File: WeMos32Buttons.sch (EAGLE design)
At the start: 9 parts, among them J1 Digital_8_13, J3 Digital_8_13

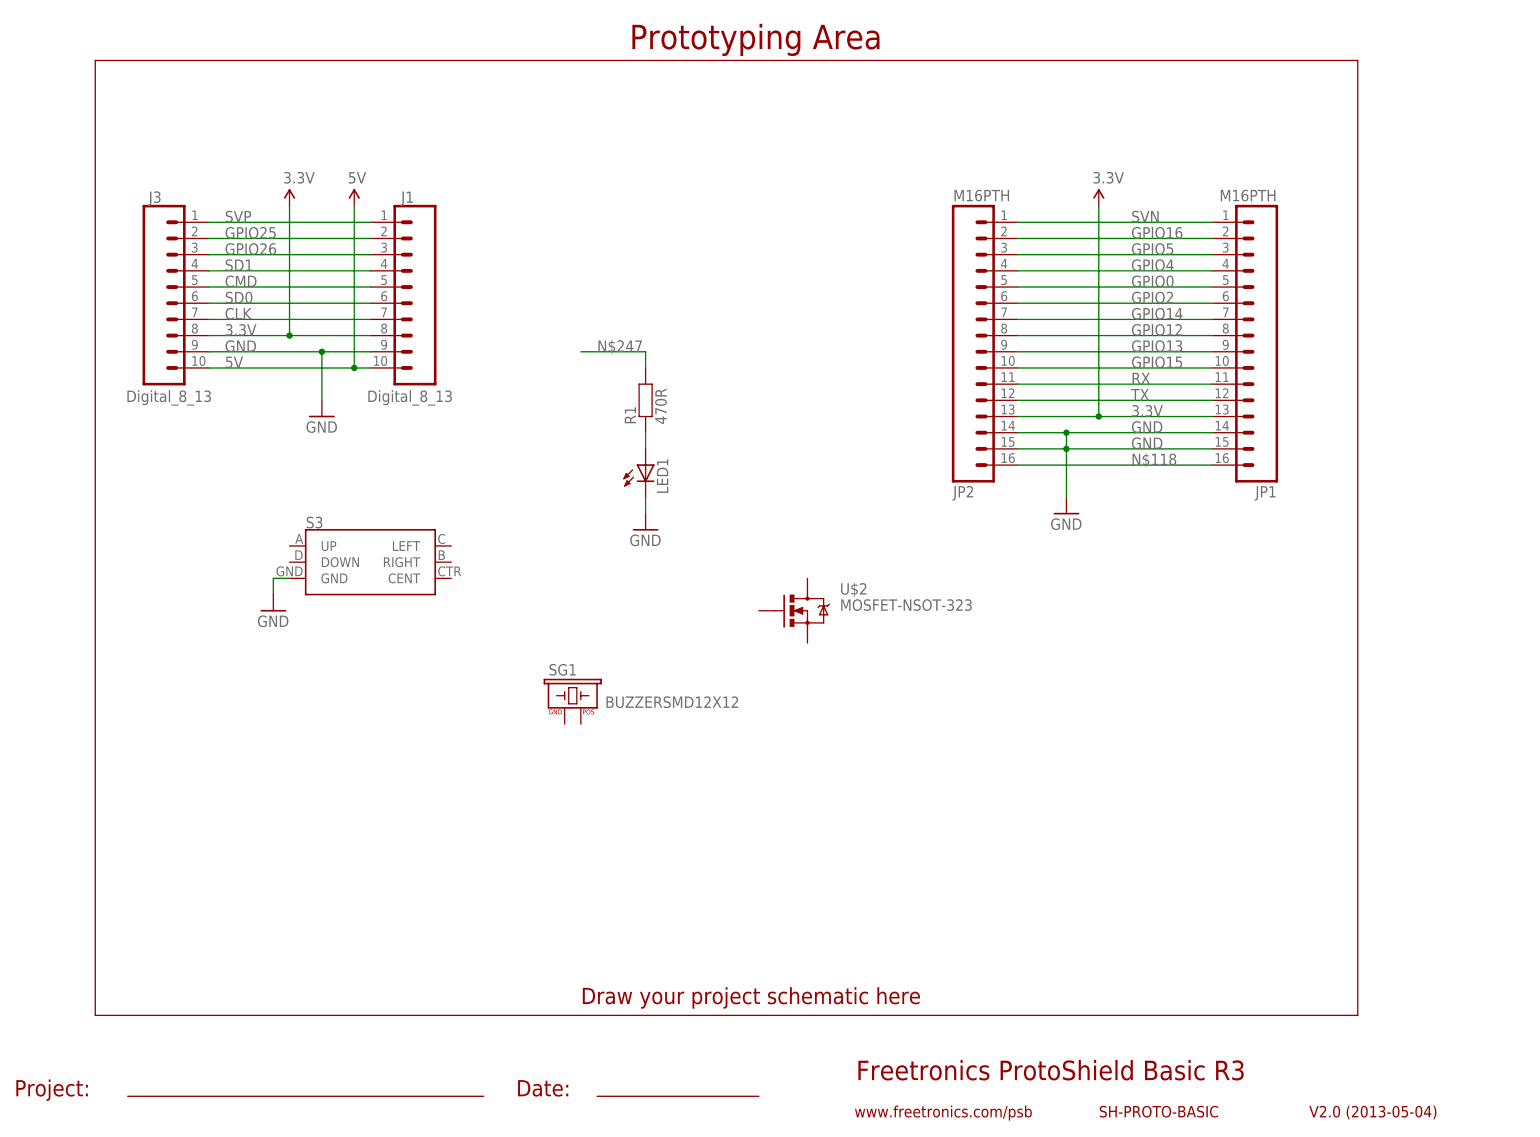
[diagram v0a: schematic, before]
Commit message: Added pull-ups on all inputs, restructured to fit fake WeMos board
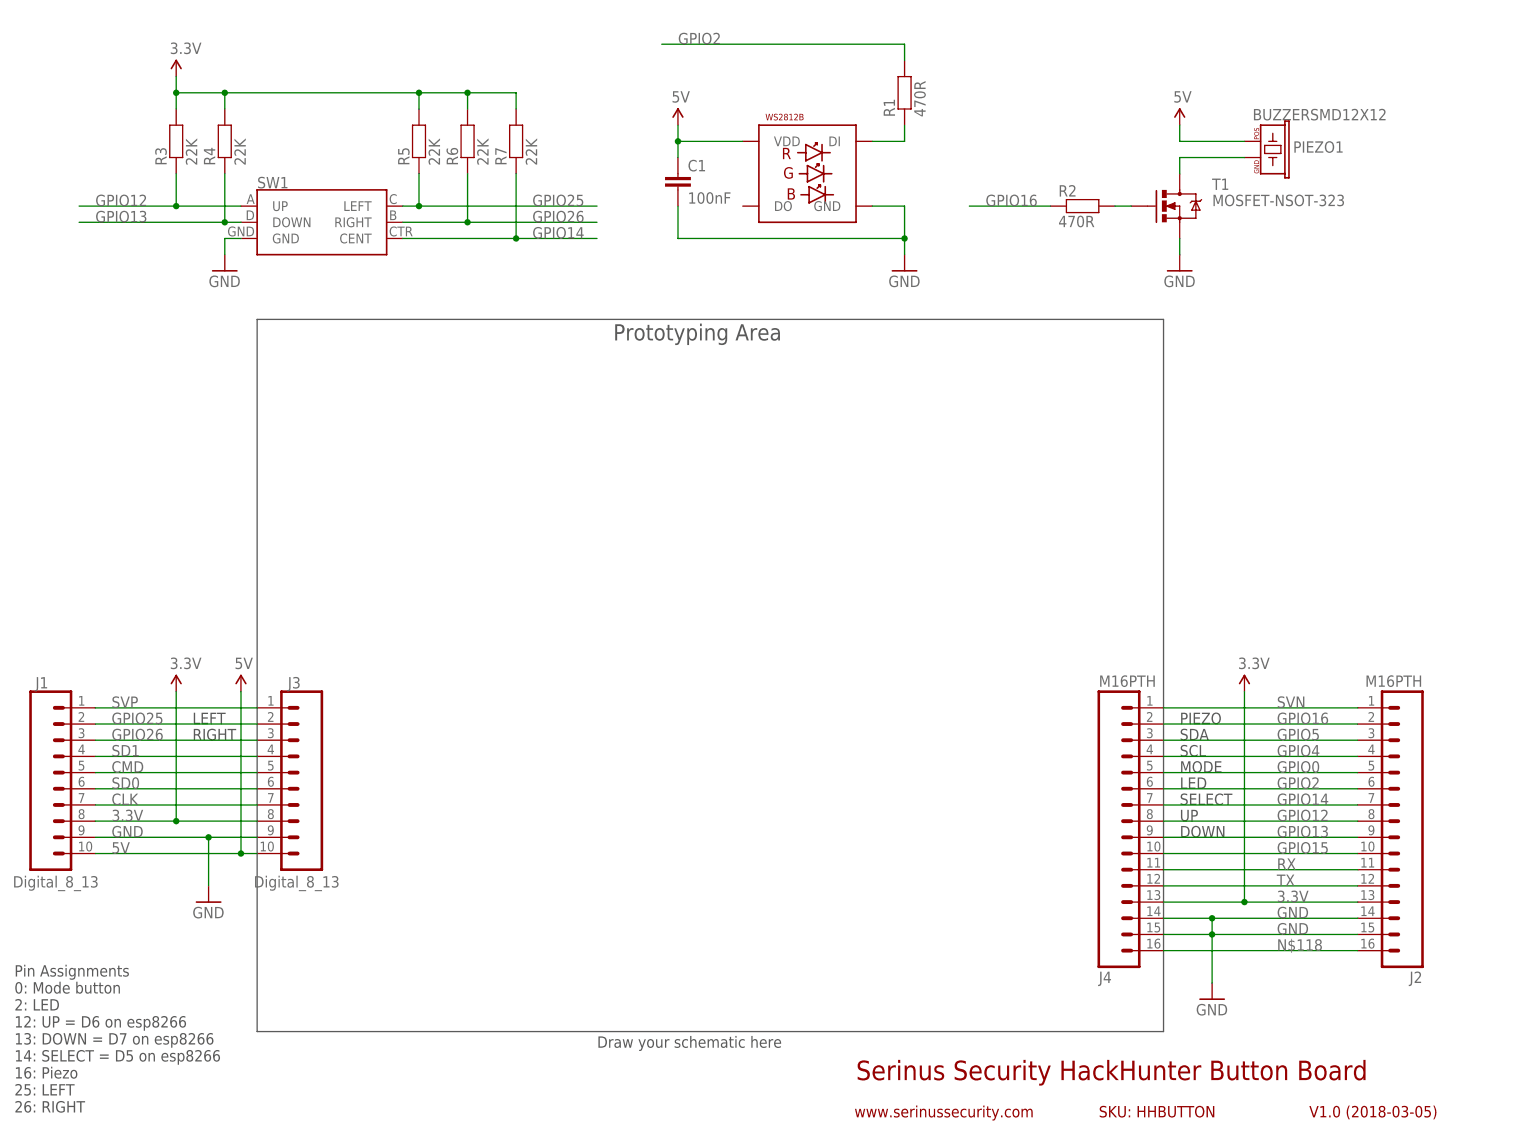
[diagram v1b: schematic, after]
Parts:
- removed JP1, JP2: M16PTH, freetronics-jon:M16PTH
- removed LED1: (no value), freetronics-jon:LED3MM
- removed S3: (no value), SparkFun-Switches:JOYSTICK_MINI
- removed SG1: BUZZERSMD12X12, freetronics-master-v1.1:BUZZERSMD12X12
- removed U$2: MOSFET-NSOT-323, freetronics-jon:MOSFET-NSOT-323
- added C1: 100nF, freetronics-jon:CAP0603
- added J2, J4: M16PTH, freetronics-jon:M16PTH
- added LED2: WS2812B5050, freetronics-jon:WS2812B5050
- added PIEZO1: BUZZERSMD12X12, freetronics-master-v1.1:BUZZERSMD12X12
- added R2: 470R, freetronics-jon:RESISTOR0603
- added R3, R4, R5, R6, R7: 22K, freetronics-jon:RESISTOR0603
- added SW1: (no value), SparkFun-Switches:JOYSTICK_MINI
- added T1: MOSFET-NSOT-323, freetronics-jon:MOSFET-NSOT-323
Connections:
- removed net N$247: R1.2
- new net N$8: PIEZO1.GND, T1.D
- new net N$9: R2.2, T1.G
- net 3.3V: now also J2.13, J4.13, R3.2, R4.2, R5.2, R6.2, R7.2; no longer JP1.13, JP2.13
- net 5V: now also C1.1, LED2.VDD, PIEZO1.POS
- net GND: now also C1.2, J2.14, J2.15, J4.14, J4.15, LED2.GND, SW1.GND, T1.S; no longer JP1.14, JP1.15, JP2.14, JP2.15, LED1.C, S3.GND
- net GPIO0: now also J2.5, J4.5; no longer JP1.5, JP2.5
- net GPIO12: now also J2.8, J4.8, R3.1, SW1.UP; no longer JP1.8, JP2.8
- net GPIO13: now also J2.9, J4.9, R4.1, SW1.DOWN; no longer JP1.9, JP2.9
- net GPIO14: now also J2.7, J4.7, R7.1, SW1.CENT; no longer JP1.7, JP2.7
- net GPIO15: now also J2.10, J4.10; no longer JP1.10, JP2.10
- net GPIO16: now also J2.2, J4.2, R2.1; no longer JP1.2, JP2.2
- net GPIO2: now also J2.6, J4.6, R1.2; no longer JP1.6, JP2.6
- net GPIO25: now also R5.1, SW1.LEFT
- net GPIO26: now also R6.1, SW1.RIGHT
- net GPIO4: now also J2.4, J4.4; no longer JP1.4, JP2.4
- net GPIO5: now also J2.3, J4.3; no longer JP1.3, JP2.3
- net N$118: now also J2.16, J4.16; no longer JP1.16, JP2.16
- net N$246: now also LED2.DI; no longer LED1.A
- net RX: now also J2.11, J4.11; no longer JP1.11, JP2.11
- net SVN: now also J2.1, J4.1; no longer JP1.1, JP2.1
- net TX: now also J2.12, J4.12; no longer JP1.12, JP2.12
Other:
- note added: "DOWN"
- note added: "Draw your schematic here"
- note added: "LED"
- note added: "LEFT"
- note added: "MODE"
- note added: "PIEZO"
- note added: "Pin Assignments 0: Mode button 2: LED 12: UP = D6 on esp8266 13: DOWN = D7 on esp8266 14: SELECT = D5 on esp8266 16: Piezo 25: LEFT 26: RIGHT"
- note added: "RIGHT"
- note added: "SCL"
- note added: "SDA"
- note added: "SELECT"
- note added: "SKU: HHBUTTON"
- note added: "Serinus Security HackHunter Button Board"
- note added: "UP"
- note added: "V1.0 (2018-03-05)"
- note added: "www.serinussecurity.com"
- note removed: "Date:"
- note removed: "Draw your project schematic here"
- note removed: "Freetronics ProtoShield Basic R3"
- note removed: "Project:"
- note removed: "SH-PROTO-BASIC"
- note removed: "V2.0 (2013-05-04)"
- note removed: "www.freetronics.com/psb"
- moved on the sheet: J1, J3, R1

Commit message: Removed branding
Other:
- note added: "SKU: ?"
- note added: "WeMos32 Button Board"
- note added: "www.freetronics.com.au"
- note removed: "SKU: HHBUTTON"
- note removed: "Serinus Security HackHunter Button Board"
- note removed: "www.serinussecurity.com"
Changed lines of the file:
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@@
 <?xml version="1.0" encoding="utf-8"?>
 <!DOCTYPE eagle SYSTEM "eagle.dtd">
-<eagle version="8.7.0">
+<eagle version="9.3.0">
 <drawing>
 <settings>
@@
 <sheet>
 <plain>
-<text x="144.78" y="12.7" size="3.048" layer="94">Serinus Security HackHunter Button Board</text>
+<text x="144.78" y="12.7" size="3.048" layer="94">WeMos32 Button Board</text>
 <text x="215.9" y="6.858" size="1.778" layer="94">V1.0 (2018-03-05)</text>
-<text x="144.526" y="6.858" size="1.778" layer="94">www.serinussecurity.com</text>
-<text x="182.88" y="6.858" size="1.778" layer="94">SKU: HHBUTTON</text>
+<text x="144.526" y="6.858" size="1.778" layer="94">www.freetronics.com.au</text>
+<text x="182.88" y="6.858" size="1.778" layer="94">SKU: ?</text>
 <frame x1="0" y1="0" x2="248.92" y2="185.42" columns="8" rows="5" layer="94"/>
 <frame x1="142.24" y1="5.08" x2="243.84" y2="17.78" columns="0" rows="0" layer="94" border-left="no" border-top="no" border-right="no" border-bottom="no"/>
@@
 <attribute name="VALUE" x="12.446" y="44.704" size="1.778" layer="96" rot="MR180"/>
 </instance>
-<instance part="GND3" gate="1" x="45.72" y="139.7"/>
-<instance part="J2" gate="G$1" x="233.68" y="50.8" rot="R180"/>
-<instance part="J4" gate="G$1" x="182.88" y="50.8" rot="MR180"/>
+<instance part="GND3" gate="1" x="45.72" y="139.7" smashed="yes">
+<attribute name="VALUE" x="43.18" y="137.16" size="1.778" layer="96"/>
+</instance>
+<instance part="J2" gate="G$1" x="233.68" y="50.8" smashed="yes" rot="R180">
+<attribute name="VALUE" x="233.68" y="76.2" size="1.778" layer="96" rot="R180"/>
+<attribute name="NAME" x="233.68" y="29.718" size="1.778" layer="95" rot="R180"/>
+</instance>
+<instance part="J4" gate="G$1" x="182.88" y="50.8" smashed="yes" rot="MR180">
+<attribute name="VALUE" x="182.88" y="76.2" size="1.778" layer="96" rot="MR180"/>
+<attribute name="NAME" x="182.88" y="29.718" size="1.778" layer="95" rot="MR180"/>
+</instance>
 <instance part="J3" gate="G$1" x="60.96" y="53.34" smashed="yes" rot="R180">
 <attribute name="NAME" x="57.658" y="75.946" size="1.778" layer="95" rot="R180"/>
 <attribute name="VALUE" x="63.754" y="44.704" size="1.778" layer="96" rot="R180"/>
 </instance>
-<instance part="U$1" gate="G$1" x="48.26" y="73.66"/>
-<instance part="P+1" gate="G$1" x="38.1" y="73.66"/>
-<instance part="GND1" gate="1" x="43.18" y="40.64"/>
-<instance part="GND2" gate="1" x="200.66" y="25.4"/>
-<instance part="P+2" gate="G$1" x="205.74" y="73.66"/>
-<instance part="SW1" gate="G$1" x="60.96" y="147.32"/>
-<instance part="GND4" gate="1" x="152.4" y="139.7"/>
-<instance part="R1" gate="G$1" x="152.4" y="167.64" rot="R90"/>
+<instance part="U$1" gate="G$1" x="48.26" y="73.66" smashed="yes">
+<attribute name="VALUE" x="47.244" y="77.216" size="1.778" layer="96"/>
+</instance>
+<instance part="P+1" gate="G$1" x="38.1" y="73.66" smashed="yes">
+<attribute name="VALUE" x="37.084" y="77.216" size="1.778" layer="96"/>
+</instance>
+<instance part="GND1" gate="1" x="43.18" y="40.64" smashed="yes">
+<attribute name="VALUE" x="40.64" y="38.1" size="1.778" layer="96"/>
+</instance>
+<instance part="GND2" gate="1" x="200.66" y="25.4" smashed="yes">
+<attribute name="VALUE" x="198.12" y="22.86" size="1.778" layer="96"/>
+</instance>
+<instance part="P+2" gate="G$1" x="205.74" y="73.66" smashed="yes">
+<attribute name="VALUE" x="204.724" y="77.216" size="1.778" layer="96"/>
+</instance>
+<instance part="SW1" gate="G$1" x="60.96" y="147.32" smashed="yes">
+<attribute name="VALUE" x="50.8" y="141.986" size="1.778" layer="96" font="vector" align="top-left"/>
+<attribute name="NAME" x="50.8" y="152.654" size="1.778" layer="95" font="vector"/>
+</instance>
+<instance part="GND4" gate="1" x="152.4" y="139.7" smashed="yes">
+<attribute name="VALUE" x="149.86" y="137.16" size="1.778" layer="96"/>
+</instance>
+<instance part="R1" gate="G$1" x="152.4" y="167.64" smashed="yes" rot="R90">
+<attribute name="NAME" x="150.9014" y="163.83" size="1.778" layer="95" rot="R90"/>
+<attribute name="VALUE" x="155.702" y="163.83" size="1.778" layer="96" rot="R90"/>
+</instance>
 <instance part="PIEZO1" gate="G$1" x="208.28" y="157.48" smashed="yes" rot="MR90">
 <attribute name="NAME" x="213.36" y="160.02" size="1.778" layer="95" rot="MR180"/>
@@
 <attribute name="VALUE" x="200.66" y="149.86" size="1.778" layer="96"/>
 </instance>
-<instance part="U$3" gate="G$1" x="195.58" y="162.56"/>
-<instance part="GND5" gate="1" x="195.58" y="139.7"/>
-<instance part="R2" gate="G$1" x="180.34" y="149.86"/>
-<instance part="R3" gate="G$1" x="38.1" y="160.02" rot="R90"/>
-<instance part="R4" gate="G$1" x="45.72" y="160.02" rot="R90"/>
-<instance part="R5" gate="G$1" x="76.2" y="160.02" rot="R90"/>
-<instance part="R6" gate="G$1" x="83.82" y="160.02" rot="R90"/>
-<instance part="R7" gate="G$1" x="91.44" y="160.02" rot="R90"/>
-<instance part="P+3" gate="G$1" x="38.1" y="170.18"/>
-<instance part="LED2" gate="G$1" x="137.16" y="154.94"/>
-<instance part="U$2" gate="G$1" x="116.84" y="162.56"/>
-<instance part="C1" gate="G$1" x="116.84" y="152.4"/>
+<instance part="U$3" gate="G$1" x="195.58" y="162.56" smashed="yes">
+<attribute name="VALUE" x="194.564" y="166.116" size="1.778" layer="96"/>
+</instance>
+<instance part="GND5" gate="1" x="195.58" y="139.7" smashed="yes">
+<attribute name="VALUE" x="193.04" y="137.16" size="1.778" layer="96"/>
+</instance>
+<instance part="R2" gate="G$1" x="180.34" y="149.86" smashed="yes">
+<attribute name="NAME" x="176.53" y="151.3586" size="1.778" layer="95"/>
+<attribute name="VALUE" x="176.53" y="146.558" size="1.778" layer="96"/>
+</instance>
+<instance part="R3" gate="G$1" x="38.1" y="160.02" smashed="yes" rot="R90">
+<attribute name="NAME" x="36.6014" y="156.21" size="1.778" layer="95" rot="R90"/>
+<attribute name="VALUE" x="41.402" y="156.21" size="1.778" layer="96" rot="R90"/>
+</instance>
+<instance part="R4" gate="G$1" x="45.72" y="160.02" smashed="yes" rot="R90">
+<attribute name="NAME" x="44.2214" y="156.21" size="1.778" layer="95" rot="R90"/>
+<attribute name="VALUE" x="49.022" y="156.21" size="1.778" layer="96" rot="R90"/>
+</instance>
+<instance part="R5" gate="G$1" x="76.2" y="160.02" smashed="yes" rot="R90">
+<attribute name="NAME" x="74.7014" y="156.21" size="1.778" layer="95" rot="R90"/>
+<attribute name="VALUE" x="79.502" y="156.21" size="1.778" layer="96" rot="R90"/>
+</instance>
+<instance part="R6" gate="G$1" x="83.82" y="160.02" smashed="yes" rot="R90">
+<attribute name="NAME" x="82.3214" y="156.21" size="1.778" layer="95" rot="R90"/>
+<attribute name="VALUE" x="87.122" y="156.21" size="1.778" layer="96" rot="R90"/>
+</instance>
+<instance part="R7" gate="G$1" x="91.44" y="160.02" smashed="yes" rot="R90">
+<attribute name="NAME" x="89.9414" y="156.21" size="1.778" layer="95" rot="R90"/>
+<attribute name="VALUE" x="94.742" y="156.21" size="1.778" layer="96" rot="R90"/>
+</instance>
+<instance part="P+3" gate="G$1" x="38.1" y="170.18" smashed="yes">
+<attribute name="VALUE" x="37.084" y="173.736" size="1.778" layer="96"/>
+</instance>
+<instance part="LED2" gate="G$1" x="137.16" y="154.94" smashed="yes"/>
+<instance part="U$2" gate="G$1" x="116.84" y="162.56" smashed="yes">
+<attribute name="VALUE" x="115.824" y="166.116" size="1.778" layer="96"/>
+</instance>
+<instance part="C1" gate="G$1" x="116.84" y="152.4" smashed="yes">
+<attribute name="NAME" x="118.364" y="155.321" size="1.778" layer="95"/>
+<attribute name="VALUE" x="118.364" y="150.241" size="1.778" layer="96"/>
+</instance>
 </instances>
 <busses>
